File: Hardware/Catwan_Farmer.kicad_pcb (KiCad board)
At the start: 2 copper layers, 67 x 77 mm, 59 parts, among them J1 SENSOR 1, J10 VSP, J2 SENSOR 2, J3 SENSOR 3, J4 BATT, J5 USB_B, J6 Conn_01x04, J7 DHT22, J9 SENSOR 4, Q1 BSS214NW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

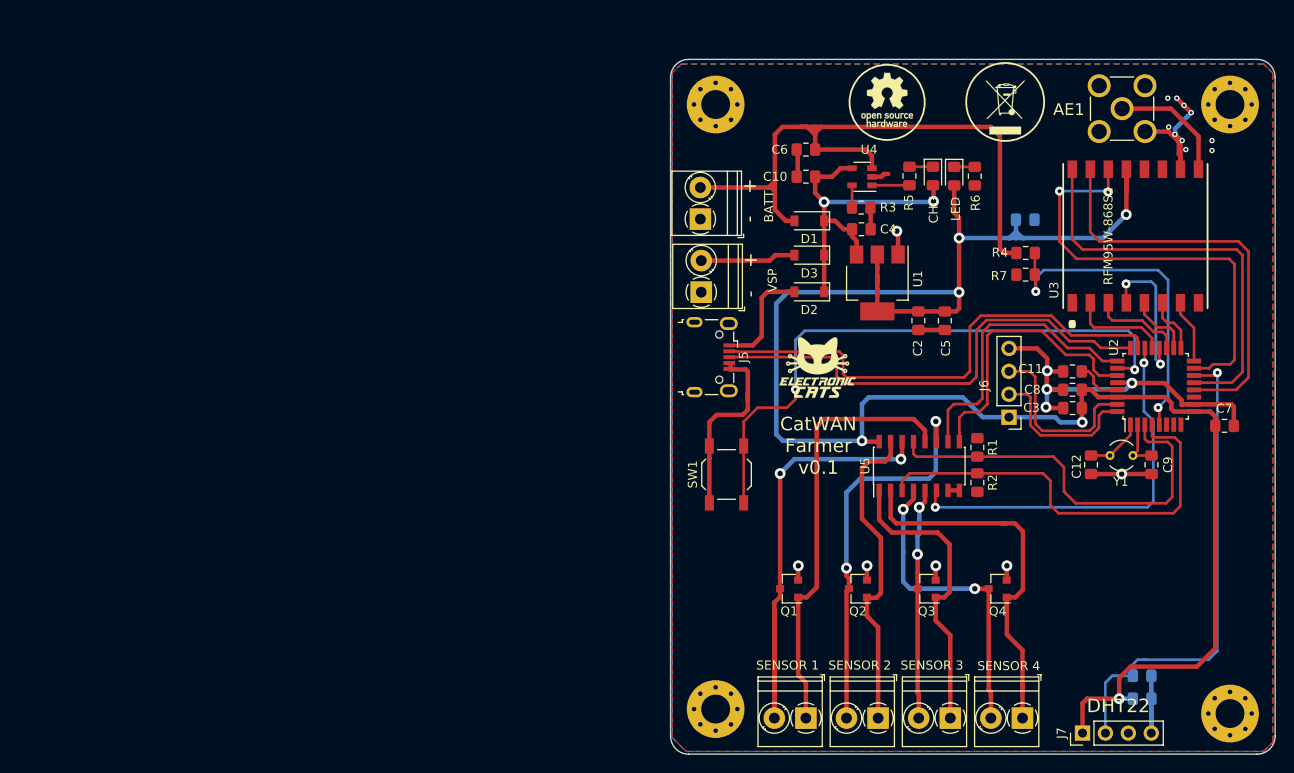
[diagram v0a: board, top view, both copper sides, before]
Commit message: add footprint crystal and value c8 and c3, fix footprint u3, u2 usb
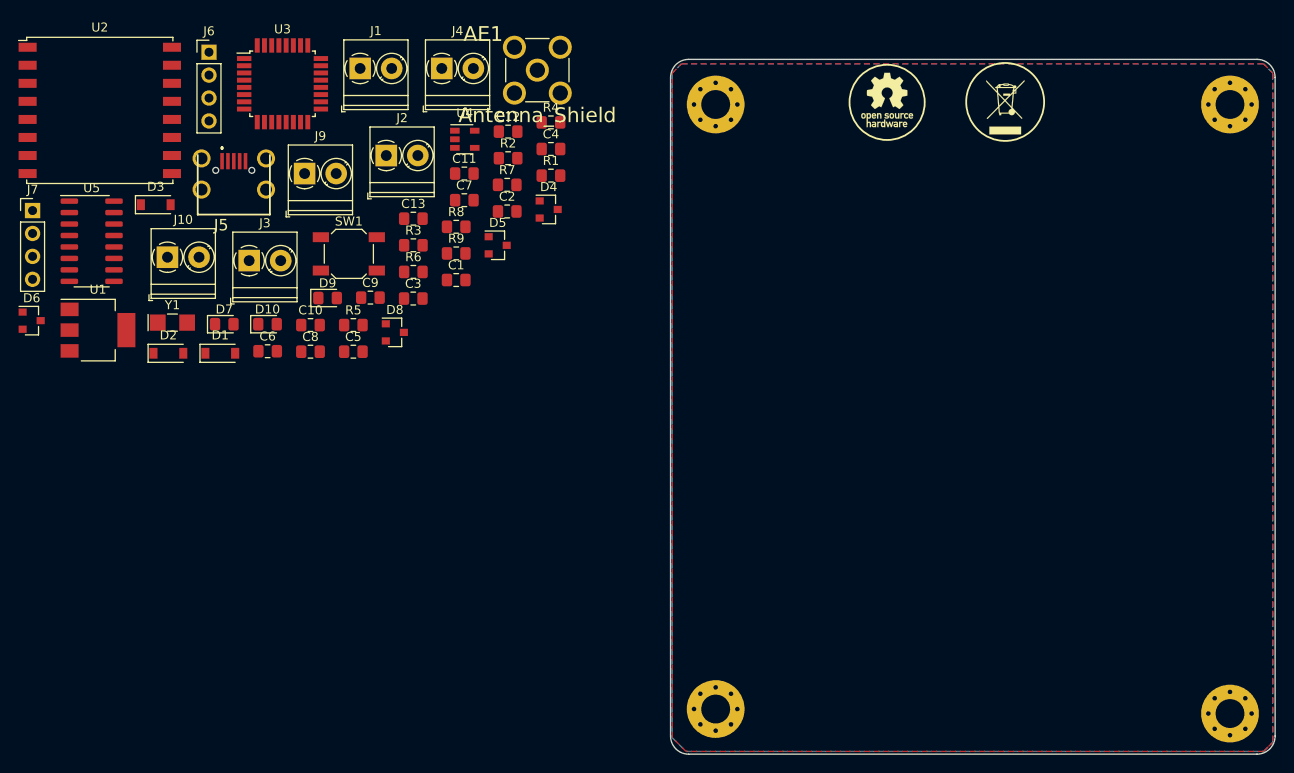
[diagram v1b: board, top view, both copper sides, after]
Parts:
- removed G***: LOGO, Aesthetics:electronic_cats_logo_8x6
- removed Q1, Q2, Q3, Q4: BSS214NW, Package_TO_SOT_SMD:SOT-23
- removed the REF*** at (165.8, 94.9)
- removed the REF*** at (153.5, 94.4)
- removed the REF*** at (136.8, 94.9)
- removed svg2mod: electronic, Aesthetics:titule_electronic_med
- added D4: AZ23C9V1, Package_TO_SOT_SMD:SOT-23, F.Cu at (93.5, 47.6)
- added D5: AZ23C9V1, Package_TO_SOT_SMD:SOT-23, F.Cu at (87.8, 51.6)
- added D6: AZ23C9V1, Package_TO_SOT_SMD:SOT-23, F.Cu at (36.2, 60.0)
- added D8: AZ23C9V1, Package_TO_SOT_SMD:SOT-23, F.Cu at (76.4, 61.3)
- added D9: LED, LED_SMD:LED_0805_2012Metric_Pad1.15x1.40mm_HandSolder, F.Cu at (69.0, 57.5)
- added R9: 1K, Resistor_SMD:R_0805_2012Metric_Pad1.15x1.40mm_HandSolder, F.Cu at (83.2, 52.5)
- C1, C13, R8: moved to F.Cu
- C12, C9: value 0.1uF -> 15pF
- J5: footprint Connector_USB:USB_Micro-B_Wuerth_629105150521 -> Connectors electroniccats:U254051N4BH806
- SW1: value RST -> SW_Push; footprint Button_Switch_SMD:SW_SPST_TL3342 -> Button_Switch_SMD:SW_SPST_SKQG_WithStem
- U2: value ATSAMD21E18A-MU -> RFM95W-915S2; footprint Package_QFP:TQFP-32_7x7mm_P0.8mm -> RF_Module:HOPERF_RFM9XW_SMD
- U3: value RFM95W-868S2 -> ATSAMD21E18A-MU; footprint Rf:RFM95W -> Package_QFP:TQFP-32_7x7mm_P0.8mm
- Y1: footprint Crystals:Crystal_AT310_d3.0mm_l10.0mm_Vertical -> Crystal:Crystal_SMD_MicroCrystal_CC7V-T1A-2Pin_3.2x1.5mm_HandSoldering
- moved J7 130.0 mm to (36.3, 47.8), turned to 0 degrees
- moved U2 120.9 mm to (43.7, 36.7), turned to 0 degrees
- moved Y1 104.9 mm to (51.8, 60.2)
- moved J9 99.9 mm to (66.4, 43.7), turned to 0 degrees
- moved J6 97.5 mm to (55.8, 30.2), turned to 0 degrees
- moved C13 96.7 mm to (78.5, 48.7)
- moved U3 96.0 mm to (64.0, 33.7), turned to 0 degrees
- moved U5 95.0 mm to (42.8, 51.2), turned to 0 degrees
- moved J3 92.8 mm to (60.3, 53.3), turned to 0 degrees
- moved R8 90.9 mm to (83.2, 49.6)
- moved C9 88.5 mm to (73.7, 57.4), turned to 0 degrees
- moved C7 87.9 mm to (84.1, 46.6)
- moved J1 87.3 mm to (72.6, 32.0), turned to 0 degrees
- moved U1 86.5 mm to (43.5, 61.0), turned to 0 degrees
- moved C8 84.6 mm to (67.1, 63.4), turned to 0 degrees
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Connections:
- U2 pad 1: /Y2 -> GND
- U2 pad 12: /DIO1 -> Net-(U2-Pad12)
- U2 pad 13: /DIO2 -> +3V3
- U2 pad 14: /DHT_DAT -> /DIO0
- U2 pad 15: /DIO0 -> /DIO1
- U2 pad 16: /DIO5 -> /DIO2
- U2 pad 2: /Y1 -> /MIS0
- U2 pad 3: /SENS_X -> /MOSI
- U2 pad 4: /SENS_Y -> /SCK
- U2 pad 5: /ADC_BAT -> /SS
- U2 pad 6: Net-(U2-Pad6) -> /RFM_RST
- U2 pad 7: Net-(U2-Pad7) -> /DIO5
- U2 pad 8: Net-(U2-Pad8) -> GND
- U2 pad 9: +3V3 -> Net-(AE1-Pad1)
- U3 pad 1: GND -> /Y2
- U3 pad 11: Net-(U3-Pad11) -> /LED
- U3 pad 12: Net-(U3-Pad12) -> /DIO1
- U3 pad 13: +3V3 -> /DIO2
- U3 pad 14: /DIO0 -> /DHT_DAT
- U3 pad 15: /DIO1 -> /DIO0
- U3 pad 16: /DIO2 -> /DIO5
- U3 pad 2: /MIS0 -> /Y1
- U3 pad 3: /MOSI -> /SENS_X
- U3 pad 4: /SCK -> /SENS_Y
- U3 pad 5: /SS -> /ADC_BAT
- U3 pad 6: /RFM_RST -> /SENS_X
- U3 pad 7: /DIO5 -> /SENS_Y
- U3 pad 8: GND -> Net-(U3-Pad8)
- U3 pad 9: Net-(AE1-Pad1) -> +3V3
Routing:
- net +3V3: track 207.0 -> 0.00 mm, vias 6 -> 0
- net GND: track 116.6 -> 0.00 mm, vias 20 -> 0
- net /BAT: track 74.1 -> 0.00 mm
- net Net-(SW1-Pad2): track 66.3 -> 0.00 mm, vias 2 -> 0
- net /D-: track 55.5 -> 0.00 mm
- net Net-(D8-Pad2): track 55.5 -> 0.00 mm, vias 2 -> 0
- net /DHT_DAT: track 54.8 -> 0.00 mm, vias 1 -> 0
- net /D+: track 54.3 -> 0.00 mm
- net /DIO0: track 49.5 -> 0.00 mm, vias 2 -> 0
- net Net-(D8-Pad1): track 48.2 -> 0.00 mm
- net /SENS_Y: track 47.7 -> 0.00 mm
- net /DIO2: track 46.2 -> 0.00 mm
- net /DIO1: track 46.0 -> 0.00 mm
- net /SENS_X: track 44.7 -> 0.00 mm
- net Net-(D5-Pad2): track 43.9 -> 0.00 mm, vias 2 -> 0
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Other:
- board text removed: "+"
- board text removed: "-"
- board text removed: "CatWAN Farmer v0.1"
- board text removed: "DHT22"

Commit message: Initial pcb
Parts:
- moved J7 128.2 mm to (150.4, 106.0), turned to 90 degrees
- moved D6 106.0 mm to (136.4, 94.5), turned to 90 degrees
- moved U2 103.7 mm to (146.4, 51.2), turned to 90 degrees
- moved Y1 97.3 mm to (147.5, 77.5)
- moved U5 94.3 mm to (131.2, 84.2), turned to 90 degrees
- moved U3 92.1 mm to (149.1, 68.8), turned to 90 degrees
- moved J2 90.6 mm to (142.3, 102.9)
- moved J3 89.1 mm to (134.3, 102.9)
- moved J1 84.3 mm to (118.2, 102.9)
- moved J9 84.2 mm to (126.3, 102.9)
- moved C9 81.0 mm to (152.2, 77.5)
- moved C7 78.1 mm to (155.9, 77.5), turned to 180 degrees
- moved D5 70.6 mm to (144.0, 94.5), turned to 90 degrees
- moved C12 66.2 mm to (142.9, 77.5), turned to 180 degrees
- moved R2 65.4 mm to (137.3, 86.0), turned to 90 degrees
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
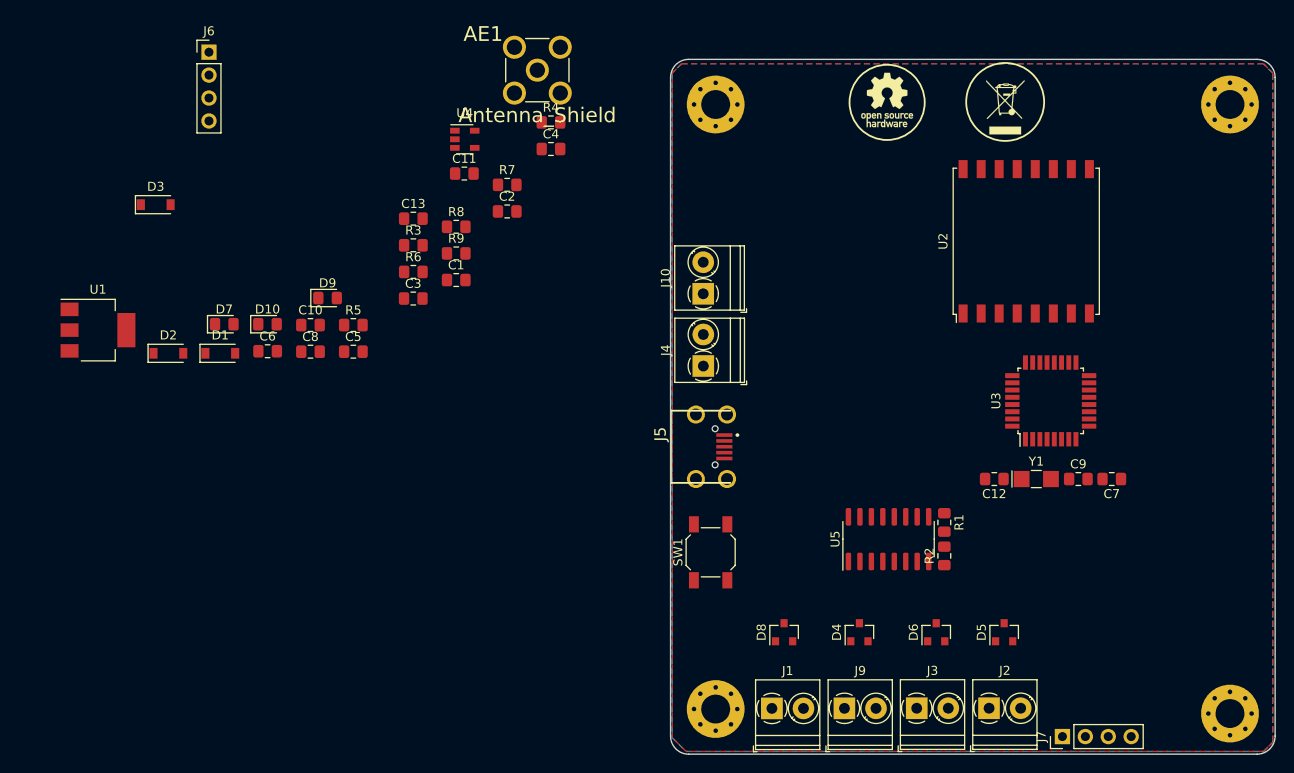
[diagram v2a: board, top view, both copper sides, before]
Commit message: End place components
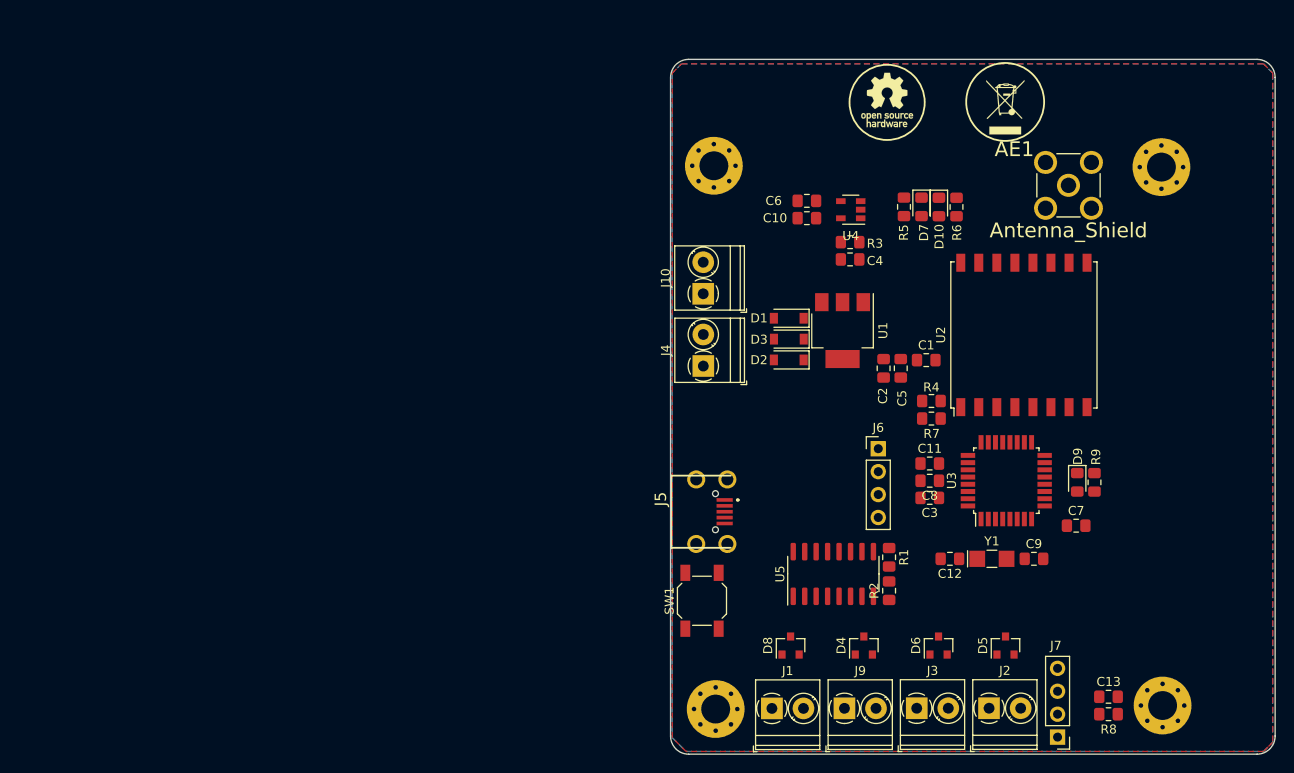
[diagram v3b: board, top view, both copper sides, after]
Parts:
- moved C13 93.5 mm to (155.5, 101.6)
- moved R8 90.2 mm to (155.5, 103.6)
- moved J6 86.2 mm to (130.0, 74.2)
- moved D9 85.6 mm to (152.1, 77.9), turned to 270 degrees
- moved U1 82.5 mm to (126.1, 61.1), turned to 270 degrees
- moved D7 78.4 mm to (134.8, 47.4), turned to 270 degrees
- moved D10 75.5 mm to (136.7, 47.4), turned to 270 degrees
- moved R9 75.1 mm to (154.0, 77.9), turned to 270 degrees
- moved D3 71.7 mm to (120.1, 62.0), turned to 180 degrees
- moved C8 70.1 mm to (135.7, 77.7), turned to 180 degrees
- moved D2 68.8 mm to (120.1, 64.3), turned to 180 degrees
- moved D1 63.1 mm to (120.1, 59.7), turned to 180 degrees
- moved R5 62.4 mm to (132.9, 47.3), turned to 90 degrees
- moved C6 62.0 mm to (122.1, 46.7)
- moved C3 61.4 mm to (135.7, 79.6), turned to 180 degrees
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
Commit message: Measure pcb
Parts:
- moved REF** 0.39 mm to (161.7, 42.7)
- moved REF** 0.30 mm to (161.6, 102.9)
- moved REF** 0.15 mm to (112.0, 42.8)

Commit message: edge cuts
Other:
- board size 67 x 77 mm -> 60 x 70 mm
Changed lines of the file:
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@@
     )
   )
+  (gr_line (start 166.99 106) (end 167 40) (layer Edge.Cuts) (width 0.15))
+  (gr_line (start 106.99 40.01) (end 107 106) (layer Edge.Cuts) (width 0.15))
+  (gr_line (start 165 38) (end 108.99 38.01) (layer Edge.Cuts) (width 0.15))
+  (gr_line (start 164.99 108) (end 109 108) (layer Edge.Cuts) (width 0.15))
   (dimension 49.79 (width 0.15) (layer Margin)
     (gr_text "49.790 mm" (at 136.985 22.35) (layer Margin)
@@
     (arrow2b (pts (xy 171.17 107.97) (xy 170.583579 106.843496)))
   )
-  (gr_arc (start 172 106) (end 172 108) (angle -90) (layer Edge.Cuts) (width 0.15))
-  (gr_arc (start 109 33) (end 109 31) (angle -90) (layer Edge.Cuts) (width 0.15))
-  (gr_arc (start 172 33) (end 174 33) (angle -90) (layer Edge.Cuts) (width 0.15))
-  (gr_line (start 109 108) (end 172 108) (layer Edge.Cuts) (width 0.15))
-  (gr_line (start 107 33) (end 107 106) (layer Edge.Cuts) (width 0.15))
-  (gr_line (start 172 31) (end 109 31) (layer Edge.Cuts) (width 0.15))
-  (gr_line (start 174 106) (end 174 33) (layer Edge.Cuts) (width 0.15))
+  (gr_arc (start 164.99 106) (end 164.99 108) (angle -90) (layer Edge.Cuts) (width 0.15))
+  (gr_arc (start 108.99 40.01) (end 108.99 38.01) (angle -90) (layer Edge.Cuts) (width 0.15))
+  (gr_arc (start 165 40) (end 167 40) (angle -90) (layer Edge.Cuts) (width 0.15))
   (gr_circle (center 131 35.765909) (end 133.54 39.067909) (layer F.SilkS) (width 0.2))
   (gr_circle (center 144.082 35.718) (end 146.114 39.528) (layer F.SilkS) (width 0.2))
@@
     (arrow2b (pts (xy 199 31) (xy 199.586421 32.126504)))
   )
+  (zone (net 2) (net_name GND) (layer F.Cu) (hatch edge 0.508)
+    (connect_pads (clearance 0.508))
+    (min_thickness 0.254)
+    (fill (arc_segments 16) (thermal_gap 0.508) (thermal_bridge_width 0.508))
+    (polygon
+      (pts
+        (xy 172.72 31.496) (xy 173.736 32.512) (xy 173.736 106.68) (xy 173.228 107.188) (xy 172.72 107.696)
+        (xy 108.712 107.696) (xy 107.188 106.172) (xy 107.188 32.512) (xy 108.204 31.496)
+      )
+    )
+  )
   (zone (net 2) (net_name GND) (layer B.Cu) (hatch edge 0.508)
     (connect_pads (clearance 0.508))
@@
       )
     )
-  )
-  (zone (net 2) (net_name GND) (layer F.Cu) (hatch edge 0.508)
-    (connect_pads (clearance 0.508))
-    (min_thickness 0.254)
-    (fill (arc_segments 16) (thermal_gap 0.508) (thermal_bridge_width 0.508))
-    (polygon
-      (pts
-        (xy 172.72 31.496) (xy 173.736 32.512) (xy 173.736 106.68) (xy 173.228 107.188) (xy 172.72 107.696)
-        (xy 108.712 107.696) (xy 107.188 106.172) (xy 107.188 32.512) (xy 108.204 31.496)
-      )
-    )
